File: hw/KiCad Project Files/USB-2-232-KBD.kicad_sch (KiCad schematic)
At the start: 48 parts, among them J1 Conn_01x05_Male, J2 USB-PINHEADER, J3 Keyboard Pin put, J4 PWR-PINH, J5 Conn_01x02_Male, P1 Keyboard, P2 USB_B_Mini, P3 DB9_Female_MountingHoles, P4 USB_A, Q1 Q_NPN_BEC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

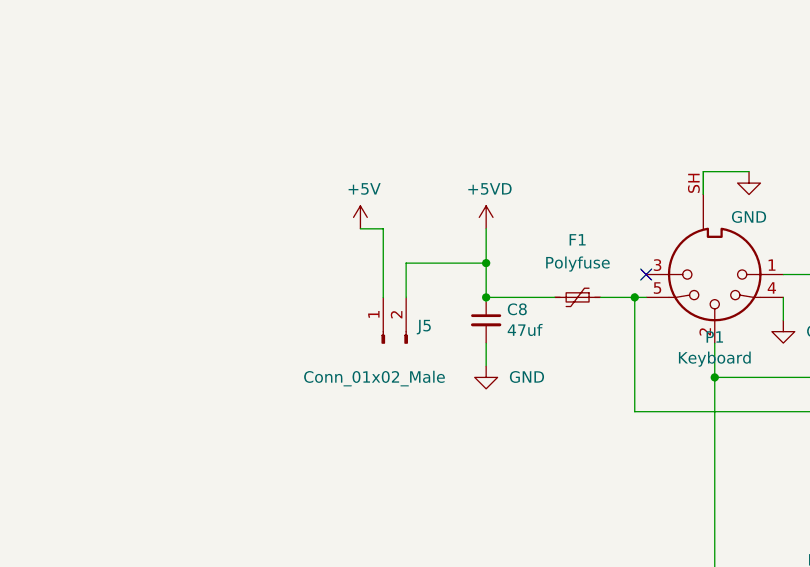
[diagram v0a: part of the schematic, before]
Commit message: Hardware update
Added a Bleed resistor. My AT machine has a bleed resistor of 150R, so I added a bleed resistor of 120K to the PCB. It shouldn't interfere with the keyboard controller nor add much to power draw but it will eventually drain the capacitors and that's all that really matters
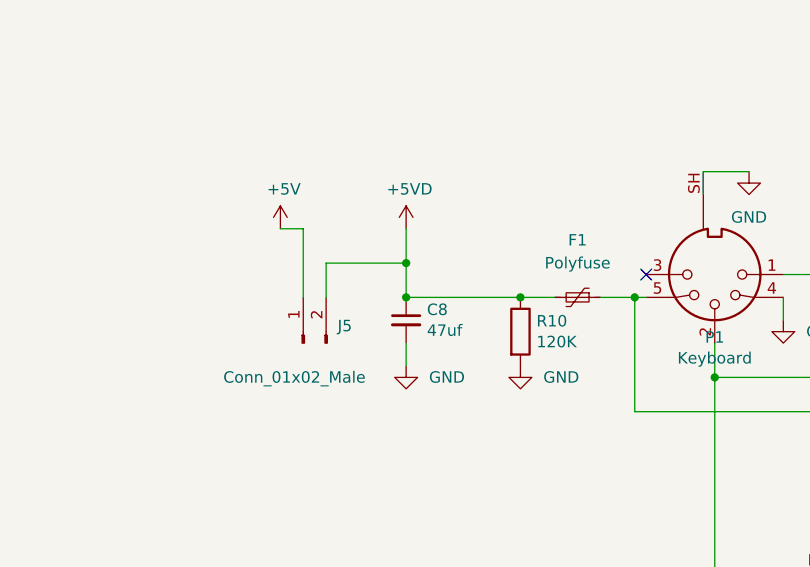
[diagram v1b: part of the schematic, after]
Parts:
- added R10: 120K, USB-2-232-KBD:R_0805_2012Metric, symbol Device:R
- R8: JLC part (none) -> C17520
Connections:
- net +5VD: now also R10.1
- net GND: now also R10.2
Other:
- moved on the sheet: C8, J5
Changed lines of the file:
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@@
   (junction (at 346.71 165.1) (diameter 0) (color 0 0 0 0)
   )
-  (junction (at 340.36 104.14) (diameter 0) (color 0 0 0 0)
+  (junction (at 331.47 104.14) (diameter 0) (color 0 0 0 0)
   )
   (junction (at 170.18 190.5) (diameter 0) (color 0 0 0 0)
@@
   (junction (at 326.39 191.77) (diameter 0) (color 0 0 0 0)
   )
-  (junction (at 340.36 107.95) (diameter 0) (color 0 0 0 0)
+  (junction (at 344.17 107.95) (diameter 0) (color 0 0 0 0)
+  )
+  (junction (at 331.47 107.95) (diameter 0) (color 0 0 0 0)
   )
   (junction (at 198.12 76.2) (diameter 0) (color 0 0 0 0)
@@
     (stroke (width 0) (type default) (color 0 0 0 0))
   )
-  (wire (pts (xy 328.93 100.33) (xy 326.39 100.33))
+  (wire (pts (xy 320.04 100.33) (xy 317.5 100.33))
     (stroke (width 0) (type default) (color 0 0 0 0))
   )
@@
     (stroke (width 0) (type default) (color 0 0 0 0))
   )
-  (wire (pts (xy 340.36 100.33) (xy 340.36 104.14))
+  (wire (pts (xy 331.47 100.33) (xy 331.47 104.14))
     (stroke (width 0) (type default) (color 0 0 0 0))
   )
@@
     (stroke (width 0) (type default) (color 0 0 0 0))
   )
-  (wire (pts (xy 331.47 104.14) (xy 340.36 104.14))
+  (wire (pts (xy 322.58 104.14) (xy 331.47 104.14))
     (stroke (width 0) (type default) (color 0 0 0 0))
   )
@@
     (stroke (width 0) (type default) (color 0 0 0 0))
   )
-  (wire (pts (xy 331.47 104.14) (xy 331.47 107.95))
+  (wire (pts (xy 322.58 104.14) (xy 322.58 107.95))
     (stroke (width 0) (type default) (color 0 0 0 0))
   )
@@
     (stroke (width 0) (type default) (color 0 0 0 0))
   )
-  (wire (pts (xy 340.36 113.03) (xy 340.36 115.57))
+  (wire (pts (xy 331.47 113.03) (xy 331.47 115.57))
     (stroke (width 0) (type default) (color 0 0 0 0))
   )
@@
     (stroke (width 0) (type default) (color 0 0 0 0))
   )
+  (wire (pts (xy 344.17 107.95) (xy 347.98 107.95))
+    (stroke (width 0) (type default) (color 0 0 0 0))
+  )
   (wire (pts (xy 294.64 158.75) (xy 247.65 158.75))
     (stroke (width 0) (type default) (color 0 0 0 0))
@@
     (stroke (width 0) (type default) (color 0 0 0 0))
   )
-  (wire (pts (xy 328.93 107.95) (xy 328.93 100.33))
+  (wire (pts (xy 320.04 107.95) (xy 320.04 100.33))
     (stroke (width 0) (type default) (color 0 0 0 0))
   )
@@
     (stroke (width 0) (type default) (color 0 0 0 0))
   )
-  (wire (pts (xy 340.36 107.95) (xy 347.98 107.95))
+  (wire (pts (xy 331.47 107.95) (xy 344.17 107.95))
     (stroke (width 0) (type default) (color 0 0 0 0))
   )
@@
     (stroke (width 0) (type default) (color 0 0 0 0))
   )
-  (wire (pts (xy 340.36 104.14) (xy 340.36 107.95))
+  (wire (pts (xy 331.47 104.14) (xy 331.47 107.95))
     (stroke (width 0) (type default) (color 0 0 0 0))
   )
@@
     (pin "2")
   )
-  (symbol (lib_id "power:+5VD") (at 340.36 100.33 0) (unit 1)
+  (symbol (lib_id "power:+5VD") (at 331.47 100.33 0) (unit 1)
     (in_bom yes) (on_board yes)
-    (property "Reference" "#PWR0109" (id 0) (at 340.36 104.14 0)
+    (property "Reference" "#PWR0109" (id 0) (at 331.47 104.14 0)
       (effects (font (size 1.27 1.27)) hide)
     )
-    (property "Value" "+5VD" (id 1) (at 340.741 95.9358 0))
-    (property "Footprint" "" (id 2) (at 340.36 100.33 0)
+    (property "Value" "+5VD" (id 1) (at 331.851 95.9358 0))
+    (property "Footprint" "" (id 2) (at 331.47 100.33 0)
       (effects (font (size 1.27 1.27)) hide)
     )
-    (property "Datasheet" "" (id 3) (at 340.36 100.33 0)
+    (property "Datasheet" "" (id 3) (at 331.47 100.33 0)
       (effects (font (size 1.27 1.27)) hide)
     )
@@
     (pin "SH")
   )
-  (symbol (lib_id "Device:C_Small") (at 340.36 110.49 0) (unit 1)
+  (symbol (lib_id "Device:C_Small") (at 331.47 110.49 0) (unit 1)
     (in_bom yes) (on_board yes)
-    (property "Reference" "C8" (id 0) (at 342.6714 109.3216 0)
+    (property "Reference" "C8" (id 0) (at 333.7814 109.3216 0)
       (effects (font (size 1.27 1.27)) (justify left))
     )
-    (property "Value" "47uf" (id 1) (at 342.6714 111.633 0)
+    (property "Value" "47uf" (id 1) (at 333.7814 111.633 0)
       (effects (font (size 1.27 1.27)) (justify left))
     )
-    (property "Footprint" "USB-2-232-KBD:C_0805_2012Metric" (id 2) (at 340.36 110.49 0)
+    (property "Footprint" "USB-2-232-KBD:C_0805_2012Metric" (id 2) (at 331.47 110.49 0)
       (effects (font (size 1.27 1.27)) hide)
     )
-    (property "Datasheet" "~" (id 3) (at 340.36 110.49 0)
+    (property "Datasheet" "~" (id 3) (at 331.47 110.49 0)
       (effects (font (size 1.27 1.27)) hide)
     )
-    (property "JLC part" "C16780" (id 4) (at 340.36 110.49 0)
+    (property "JLC part" "C16780" (id 4) (at 331.47 110.49 0)
       (effects (font (size 1.27 1.27)) hide)
     )
@@
       (effects (font (size 1.27 1.27)) hide)
     )
+    (property "JLC part" "C17520" (id 4) (at 368.3 195.58 0)
+      (effects (font (size 1.27 1.27)) hide)
+    )
     (pin "1")
     (pin "2")
@@
     (pin "1")
   )
+  (symbol (lib_id "Device:R") (at 344.17 111.76 0) (unit 1)
+    (in_bom yes) (on_board yes)
+    (property "Reference" "R10" (id 0) (at 345.948 110.5916 0)
+      (effects (font (size 1.27 1.27)) (justify left))
+    )
+    (property "Value" "120K" (id 1) (at 345.948 112.903 0)
+      (effects (font (size 1.27 1.27)) (justify left))
+    )
+    (property "Footprint" "USB-2-232-KBD:R_0805_2012Metric" (id 2) (at 342.392 111.76 90)
+      (effects (font (size 1.27 1.27)) hide)
+    )
+    (property "Datasheet" "~" (id 3) (at 344.17 111.76 0)
+      (effects (font (size 1.27 1.27)) hide)
+    )
+    (property "JLC Part" "C17436" (id 4) (at 344.17 111.76 0)
+      (effects (font (size 1.27 1.27)) hide)
+    )
+    (pin "1")
+    (pin "2")
+  )
   (symbol (lib_id "power:GND") (at 327.66 157.2558 0) (unit 1)
     (in_bom yes) (on_board yes) (fields_autoplaced)
@@
     (pin "1")
   )
-  (symbol (lib_id "Connector:Conn_01x02_Male") (at 328.93 113.03 90) (unit 1)
+  (symbol (lib_id "Connector:Conn_01x02_Male") (at 320.04 113.03 90) (unit 1)
     (in_bom yes) (on_board yes)
-    (property "Reference" "J5" (id 0) (at 332.74 111.1249 90)
+    (property "Reference" "J5" (id 0) (at 323.85 111.1249 90)
       (effects (font (size 1.27 1.27)) (justify right))
     )
-    (property "Value" "Conn_01x02_Male" (id 1) (at 320.04 116.84 90)
+    (property "Value" "Conn_01x02_Male" (id 1) (at 311.15 116.84 90)
       (effects (font (size 1.27 1.27)) (justify right))
     )
-    (property "Footprint" "USB-2-232-KBD:PinHeader_PWR_FROM_AT" (id 2) (at 328.93 113.03 0)
+    (property "Footprint" "USB-2-232-KBD:PinHeader_PWR_FROM_AT" (id 2) (at 320.04 113.03 0)
       (effects (font (size 1.27 1.27)) hide)
     )
-    (property "Datasheet" "~" (id 3) (at 328.93 113.03 0)
+    (property "Datasheet" "~" (id 3) (at 320.04 113.03 0)
       (effects (font (size 1.27 1.27)) hide)
     )
@@
     (pin "1")
   )
+  (symbol (lib_id "power:GND") (at 344.17 115.57 0) (unit 1)
+    (in_bom yes) (on_board yes) (fields_autoplaced)
+    (property "Reference" "#PWR0149" (id 0) (at 344.17 121.92 0)
+      (effects (font (size 1.27 1.27)) hide)
+    )
+    (property "Value" "GND" (id 1) (at 346.71 116.8399 0)
+      (effects (font (size 1.27 1.27)) (justify left))
+    )
+    (property "Footprint" "" (id 2) (at 344.17 115.57 0)
+      (effects (font (size 1.27 1.27)) hide)
+    )
+    (property "Datasheet" "" (id 3) (at 344.17 115.57 0)
+      (effects (font (size 1.27 1.27)) hide)
+    )
+    (pin "1")
+  )
   (symbol (lib_id "power:GND") (at 214.63 123.19 270) (unit 1)
     (in_bom yes) (on_board yes) (fields_autoplaced)
@@
     (pin "1")
   )
-  (symbol (lib_id "power:GND") (at 340.36 115.57 0) (unit 1)
+  (symbol (lib_id "power:GND") (at 331.47 115.57 0) (unit 1)
     (in_bom yes) (on_board yes) (fields_autoplaced)
-    (property "Reference" "#PWR0136" (id 0) (at 340.36 121.92 0)
+    (property "Reference" "#PWR0136" (id 0) (at 331.47 121.92 0)
       (effects (font (size 1.27 1.27)) hide)
     )
-    (property "Value" "GND" (id 1) (at 342.9 116.8399 0)
+    (property "Value" "GND" (id 1) (at 334.01 116.8399 0)
       (effects (font (size 1.27 1.27)) (justify left))
     )
-    (property "Footprint" "" (id 2) (at 340.36 115.57 0)
+    (property "Footprint" "" (id 2) (at 331.47 115.57 0)
       (effects (font (size 1.27 1.27)) hide)
     )
-    (property "Datasheet" "" (id 3) (at 340.36 115.57 0)
+    (property "Datasheet" "" (id 3) (at 331.47 115.57 0)
       (effects (font (size 1.27 1.27)) hide)
     )
     (pin "1")
   )
-  (symbol (lib_id "power:+5V") (at 326.39 100.33 0) (unit 1)
+  (symbol (lib_id "power:+5V") (at 317.5 100.33 0) (unit 1)
     (in_bom yes) (on_board yes)
-    (property "Reference" "#PWR0151" (id 0) (at 326.39 104.14 0)
+    (property "Reference" "#PWR0151" (id 0) (at 317.5 104.14 0)
       (effects (font (size 1.27 1.27)) hide)
     )
-    (property "Value" "+5V" (id 1) (at 326.771 95.9358 0))
-    (property "Footprint" "" (id 2) (at 326.39 100.33 0)
+    (property "Value" "+5V" (id 1) (at 317.881 95.9358 0))
+    (property "Footprint" "" (id 2) (at 317.5 100.33 0)
       (effects (font (size 1.27 1.27)) hide)
     )
-    (property "Datasheet" "" (id 3) (at 326.39 100.33 0)
+    (property "Datasheet" "" (id 3) (at 317.5 100.33 0)
       (effects (font (size 1.27 1.27)) hide)
     )
@@
       (reference "#PWR0148") (unit 1) (value "+5V") (footprint "")
     )
+    (path "/4bc4c02d-e71c-43c9-94e3-3ab89d09f52a"
+      (reference "#PWR0149") (unit 1) (value "GND") (footprint "")
+    )
     (path "/0001ef74-e985-473c-961c-d2d6f6b441ba"
       (reference "#PWR0150") (unit 1) (value "GND") (footprint "")
@@
       (reference "R9") (unit 1) (value "1K") (footprint "USB-2-232-KBD:R_0402_LEDS")
     )
+    (path "/279bc97b-2cce-4cf0-8ad4-0c8bba939cb4"
+      (reference "R10") (unit 1) (value "120K") (footprint "USB-2-232-KBD:R_0805_2012Metric")
+    )
     (path "/00000000-0000-0000-0000-0000619452df"
